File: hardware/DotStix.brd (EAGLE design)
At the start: 20.3 x 50 mm, 27 parts, among them IC2 SI1145, U1 ATMEGA328P-MU-QFN32, U2 TMP102

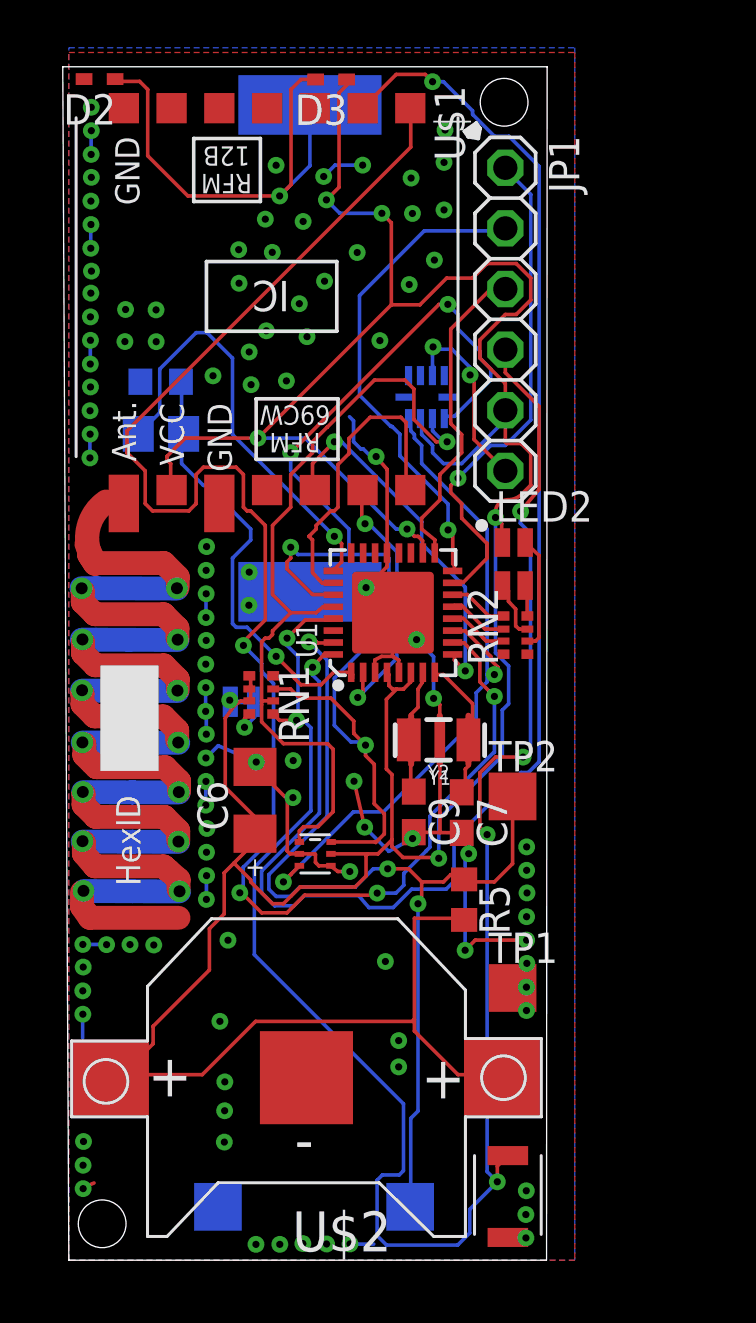
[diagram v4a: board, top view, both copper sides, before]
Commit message: Draft: add 9DoF motion sensor
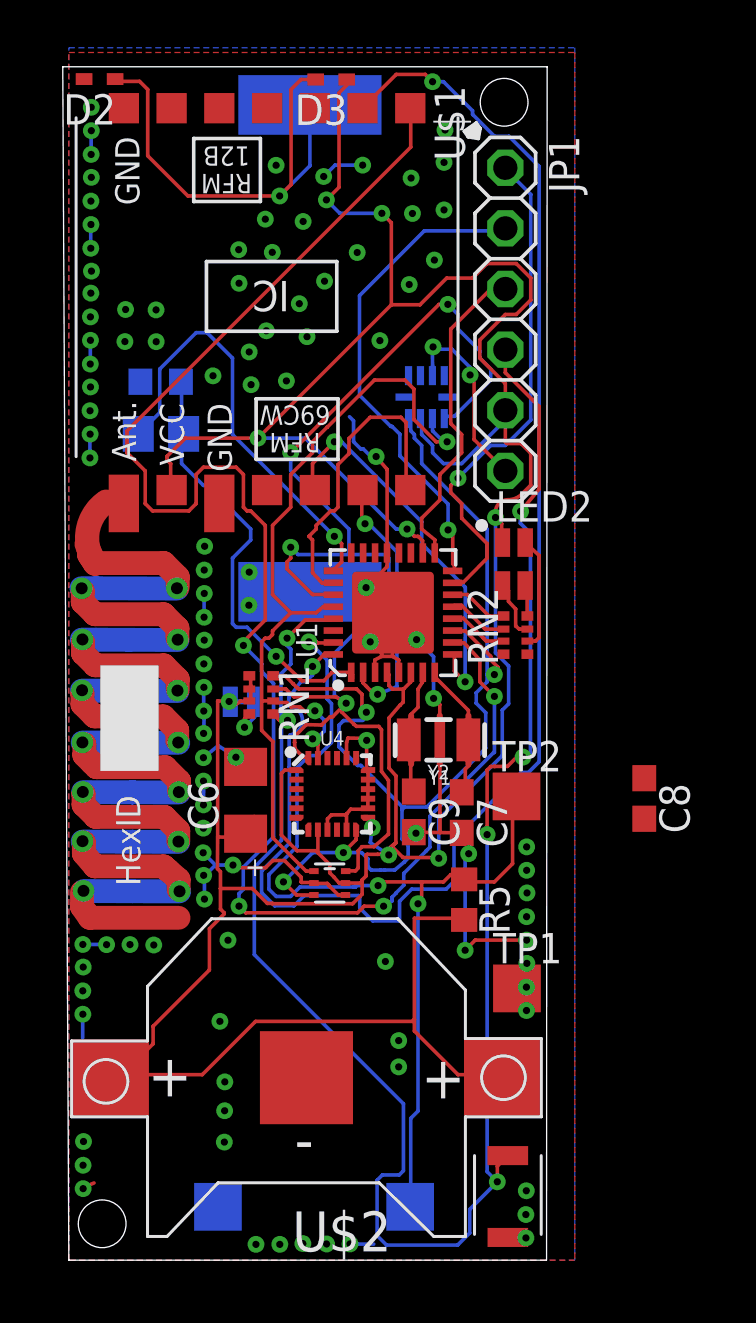
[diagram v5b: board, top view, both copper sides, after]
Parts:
- added C8: 0.1uF, resistor:C0603
- added U4: 9DoF IMU, SparkFun-Sensors:QFN24-3X3
- moved U2 1.37 mm to (10.9, 15.8)
- moved C6 0.39 mm to (7.41, 19.3)
- moved TP1 0.18 mm to (18.8, 11.4)
- moved TP2 0.17 mm to (18.8, 19.4)
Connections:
- new net N$11: C8.1, U4.10
- net +3V3: now also U4.1, U4.13, U4.8
- net GND: now also C8.2, U4.11, U4.18, U4.20, U4.9
- net INT_MULTIPLE: now also RN1.4, U4.12
- net SCL: now also U4.23
- net SDA: now also U4.24
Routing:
- net INT_MULTIPLE: track 29.3 -> 45.6 mm, vias 2 -> 4
- net +3V3: track 144.9 -> 158.2 mm, vias 7 -> 9
- net GND: track 71.9 -> 76.5 mm, vias 112 -> 110
- net SDA: track 49.8 -> 53.4 mm
- net SCL: track 33.8 -> 37.4 mm, vias 1 -> 3
- net XTAL2: track 5.11 -> 3.80 mm
- net RIRQ: track 62.1 -> 63.2 mm
- net RSDI: track 15.4 -> 16.3 mm
- net RST: track 79.6 -> 78.7 mm

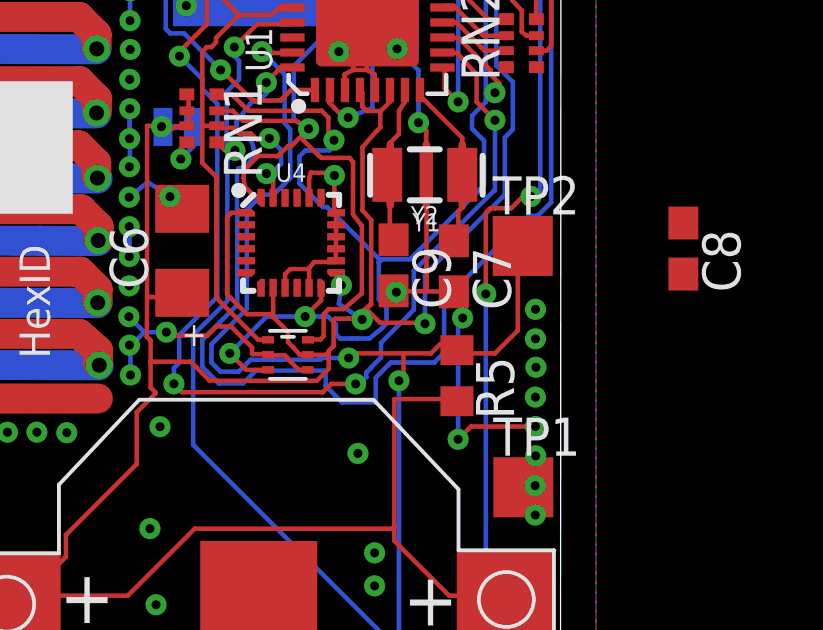
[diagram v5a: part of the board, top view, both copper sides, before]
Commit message: Draft:  9DoF pins connected, need to fix warnings
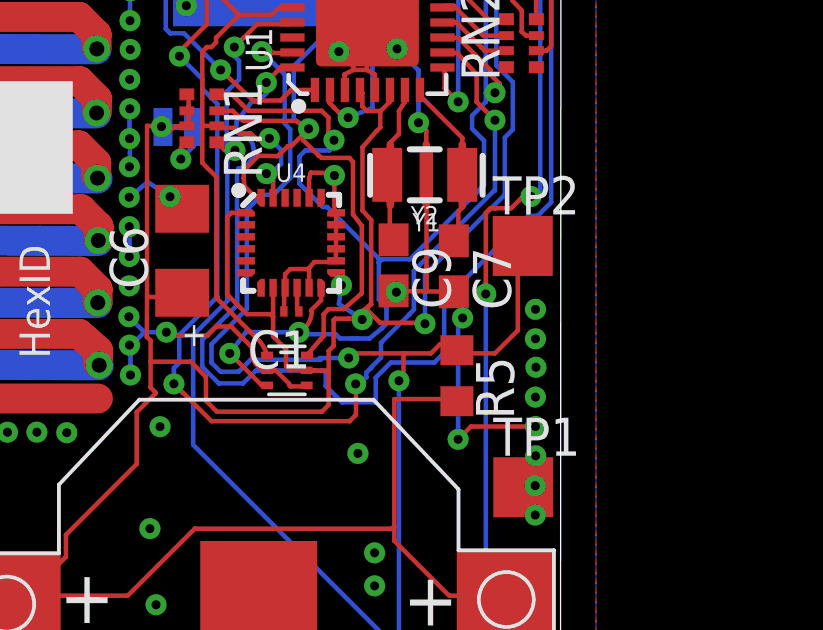
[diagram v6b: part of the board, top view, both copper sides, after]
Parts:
- removed C8: 0.1uF, resistor:C0603
- added C1: 0.1uF, rcl:C0201
- RN1: value (none) -> 4.7kΩ
- moved U2 0.52 mm to (10.9, 15.3)
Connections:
- net GND: now also C1.2; no longer C8.2
- net N$11: now also C1.1; no longer C8.1
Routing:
- net +3V3: track 158.2 -> 160.9 mm
- net RSDO: track 68.0 -> 69.4 mm
- net GND: track 76.5 -> 77.5 mm
- net N$11: track 0.00 -> 0.81 mm

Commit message: Add 9Dof: removed warnings
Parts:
- moved TP2 0.20 mm to (18.6, 19.4)
- moved TP1 0.20 mm to (18.6, 11.4)
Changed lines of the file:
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@@
 <element name="U$2" library="adafruit" package="CR1220-SMD" value="" x="9.9568" y="7.6454" rot="R180"/>
 <element name="JP1" library="adafruit" package="1X06" value="" x="18.288" y="39.4208" rot="R270"/>
-<element name="TP1" library="testpad" package="TP20SQ" value="TPTP20SQ" x="18.77568125" y="11.38681875">
-<attribute name="TP_SIGNAL_NAME" value="" x="18.77568125" y="11.38681875" size="1.778" layer="27" display="off"/>
+<element name="TP1" library="testpad" package="TP20SQ" value="TPTP20SQ" x="18.580103125" y="11.389359375">
+<attribute name="TP_SIGNAL_NAME" value="" x="18.580103125" y="11.389359375" size="1.778" layer="27" display="off"/>
 </element>
-<element name="TP2" library="testpad" package="TP20SQ" value="TPTP20SQ" x="18.7579" y="19.431">
-<attribute name="TP_SIGNAL_NAME" value="" x="18.7579" y="19.431" size="1.778" layer="27" display="off"/>
+<element name="TP2" library="testpad" package="TP20SQ" value="TPTP20SQ" x="18.56231875" y="19.433540625">
+<attribute name="TP_SIGNAL_NAME" value="" x="18.56231875" y="19.433540625" size="1.778" layer="27" display="off"/>
 </element>
 <element name="D1" library="SparkFun" package="SOLARBIT-12X1" value="SOLAR-IXYS-" x="10.101578125" y="38.204140625" rot="MR270"/>
@@
 <wire x1="8.5471" y1="16.74621875" x2="8.244840625" y2="16.443959375" width="0.1524" layer="1"/>
 <wire x1="8.244840625" y1="16.443959375" x2="6.990078125" y2="16.443959375" width="0.1524" layer="1"/>
-<wire x1="6.990078125" y1="16.443959375" x2="6.87831875" y2="16.55571875" width="0.1524" layer="1"/>
-<via x="6.87831875" y="16.55571875" extent="1-16" drill="0.3"/>
-<wire x1="6.87831875" y1="16.55571875" x2="6.1442625" y2="16.55571875" width="0.1524" layer="16"/>
+<wire x1="6.990078125" y1="16.443959375" x2="6.830059375" y2="16.197578125" width="0.1524" layer="1"/>
+<via x="6.830059375" y="16.197578125" extent="1-16" drill="0.3"/>
+<wire x1="6.830059375" y1="16.197578125" x2="6.1442625" y2="16.55571875" width="0.1524" layer="16"/>
 <wire x1="6.1442625" y1="16.55571875" x2="5.628640625" y2="17.071340625" width="0.1524" layer="16"/>
 <wire x1="5.68198125" y1="16.12391875" x2="5.7124625" y2="16.12391875" width="0.1524" layer="16"/>
@@
 <wire x1="18.288" y1="37.1856" x2="18.288" y2="38.1508" width="0.1524" layer="1"/>
 <wire x1="19.6977" y1="35.7759" x2="18.288" y2="37.1856" width="0.1524" layer="1"/>
-<wire x1="17.526" y1="17.8308" x2="17.490440625" y2="18.150840625" width="0.1524" layer="1"/>
+<wire x1="17.526" y1="17.8308" x2="17.490440625" y2="18.150840625" width="0" layer="19" extent="1-16"/>
 <wire x1="17.526" y1="3.7109375" x2="17.526" y2="17.8308" width="0.1524" layer="16"/>
 <via x="9.144" y="26.0604" extent="1-16" drill="0.3"/>
@@
 <wire x1="18.3769" y1="20.6883" x2="17.846040625" y2="20.6883" width="0.1524" layer="1"/>
 <wire x1="17.846040625" y1="20.6883" x2="17.8435" y2="20.685759375" width="0.1524" layer="1"/>
-<wire x1="17.8435" y1="20.685759375" x2="17.6784" y2="20.685759375" width="0.1524" layer="1"/>
-<wire x1="17.6784" y1="20.685759375" x2="17.526" y2="20.533359375" width="0.1524" layer="1"/>
-<wire x1="17.526" y1="20.533359375" x2="17.526" y2="17.8308" width="0.1524" layer="1"/>
 <wire x1="7.7724" y1="16.4592" x2="8.91031875" y2="17.59711875" width="0.1524" layer="16"/>
 <wire x1="8.91031875" y1="17.59711875" x2="8.91031875" y2="22.34691875" width="0.1524" layer="16"/>
@@
 <wire x1="8.887459375" y1="24.56688125" x2="8.887459375" y2="22.616159375" width="0.1524" layer="16"/>
 <wire x1="8.887459375" y1="22.616159375" x2="9.16431875" y2="22.616159375" width="0.1524" layer="16"/>
+<wire x1="17.8435" y1="20.685759375" x2="17.447259375" y2="20.685759375" width="0.1524" layer="1"/>
+<wire x1="17.447259375" y1="20.685759375" x2="17.2974" y2="20.5359" width="0.1524" layer="1"/>
+<wire x1="17.2974" y1="20.5359" x2="17.2974" y2="18.0594" width="0.1524" layer="1"/>
+<wire x1="17.2974" y1="18.0594" x2="17.526" y2="17.8308" width="0.1524" layer="1"/>
 </signal>
 <signal name="RSEL">
@@
 <via x="17.8308" y="23.622" extent="1-16" drill="0.3"/>
 <via x="7.3152" y="25.7556" extent="1-16" drill="0.3"/>
-<wire x1="7.30758125" y1="16.46428125" x2="7.30758125" y2="15.53718125" width="0.1524" layer="16"/>
 <wire x1="17.8308" y1="21.2725" x2="17.8308" y2="23.622" width="0.1524" layer="16"/>
 <wire x1="17.8308" y1="21.2725" x2="17.800321875" y2="21.2725" width="0.1524" layer="16"/>
@@
 <wire x1="8.0772" y1="24.665940625" x2="8.57758125" y2="24.165559375" width="0.1524" layer="16"/>
 <wire x1="8.57758125" y1="24.165559375" x2="8.57758125" y2="17.73428125" width="0.1524" layer="16"/>
-<wire x1="8.57758125" y1="17.73428125" x2="7.30758125" y2="16.46428125" width="0.1524" layer="16"/>
 <wire x1="13.7033" y1="15.3797" x2="13.7033" y2="15.367" width="0.1524" layer="16"/>
 <wire x1="13.7033" y1="15.367" x2="13.54328125" y2="15.20698125" width="0.1524" layer="16"/>
@@
 <wire x1="13.197840625" y1="13.79981875" x2="13.197840625" y2="14.8209" width="0.1524" layer="1"/>
 <wire x1="13.197840625" y1="14.8209" x2="13.18768125" y2="14.831059375" width="0.1524" layer="1"/>
+<wire x1="7.30758125" y1="15.53718125" x2="7.30758125" y2="15.547340625" width="0.1524" layer="16"/>
+<wire x1="7.30758125" y1="15.547340625" x2="7.4422" y2="15.681959375" width="0.1524" layer="16"/>
+<wire x1="7.4422" y1="15.681959375" x2="7.4422" y2="16.5989" width="0.1524" layer="16"/>
+<wire x1="7.4422" y1="16.5989" x2="8.57758125" y2="17.73428125" width="0.1524" layer="16"/>
 </signal>
 <signal name="RIRQ">
@@
 <contactref element="U4" pad="8"/>
 <wire x1="12.28851875" y1="15.930878125" x2="12.45361875" y2="16.095978125" width="0.1524" layer="1"/>
-<wire x1="6.2255375" y1="16.40331875" x2="6.2357" y2="17.731740625" width="0.1524" layer="1"/>
-<wire x1="6.2357" y1="17.731740625" x2="6.2357" y2="23.434040625" width="0.1524" layer="1"/>
+<wire x1="6.240778125" y1="16.40331875" x2="6.238240625" y2="17.731740625" width="0.1524" layer="1"/>
+<wire x1="6.238240625" y1="17.731740625" x2="6.2357" y2="23.434040625" width="0.1524" layer="1"/>
 <wire x1="6.2357" y1="23.434040625" x2="6.715759375" y2="23.408640625" width="0.1524" layer="1"/>
 <via x="6.715759375" y="23.408640625" extent="1-16" drill="0.3"/>
@@
 <wire x1="6.581140625" y1="23.41118125" x2="6.76401875" y2="23.395940625" width="0.1524" layer="16"/>
 <wire x1="7.62" y1="17.34058125" x2="7.25678125" y2="17.7038" width="0.1524" layer="1"/>
-<wire x1="7.25678125" y1="17.7038" x2="6.2357" y2="17.731740625" width="0.1524" layer="1"/>
+<wire x1="7.25678125" y1="17.7038" x2="6.238240625" y2="17.731740625" width="0.1524" layer="1"/>
 <wire x1="10.43630625" y1="18.035140625" x2="10.43630625" y2="17.069353125" width="0.1524" layer="1"/>
 <wire x1="12.58880625" y1="18.535140625" x2="12.70761875" y2="18.535140625" width="0.1524" layer="1"/>
-<wire x1="12.70761875" y1="18.535140625" x2="12.715240625" y2="18.1229" width="0.1524" layer="1"/>
-<via x="12.715240625" y="18.1229" extent="1-16" drill="0.3"/>
-<wire x1="12.715240625" y1="18.1229" x2="12.62888125" y2="17.498059375" width="0.1524" layer="16"/>
+<wire x1="12.70761875" y1="18.535140625" x2="12.7736625" y2="18.176240625" width="0.1524" layer="1"/>
+<via x="12.7736625" y="18.176240625" extent="1-16" drill="0.3"/>
+<wire x1="12.7736625" y1="18.176240625" x2="12.62888125" y2="17.498059375" width="0.1524" layer="16"/>
 <wire x1="12.62888125" y1="17.498059375" x2="13.40358125" y2="16.979896875" width="0.1524" layer="16"/>
 <via x="13.40358125" y="16.979896875" extent="1-16" drill="0.3"/>
@@
 <wire x1="6.51001875" y1="14.554203125" x2="6.352540625" y2="14.71168125" width="0.1524" layer="1"/>
 <wire x1="6.352540625" y1="14.71168125" x2="6.352540625" y2="15.572740625" width="0.1524" layer="1"/>
-<wire x1="6.352540625" y1="15.572740625" x2="6.352540625" y2="16.276315625" width="0.1524" layer="1"/>
-<wire x1="6.352540625" y1="16.276315625" x2="6.2255375" y2="16.40331875" width="0.1524" layer="1"/>
 <wire x1="7.69111875" y1="15.572740625" x2="6.352540625" y2="15.572740625" width="0.1524" layer="1"/>
 <wire x1="9.48380625" y1="20.535140625" x2="9.046721875" y2="20.535140625" width="0.1524" layer="1"/>
@@
 <wire x1="10.99311875" y1="15.288259375" x2="11.55151875" y2="15.288259375" width="0.1524" layer="1"/>
 <wire x1="11.55151875" y1="15.288259375" x2="11.5566" y2="15.283178125" width="0.1524" layer="1"/>
+<wire x1="6.240778125" y1="16.40331875" x2="6.23315625" y2="15.69974375" width="0.1524" layer="1"/>
+<wire x1="6.23315625" y1="15.69974375" x2="6.352540625" y2="15.572740625" width="0.1524" layer="1"/>
 <wire x1="6.76401875" y1="23.395940625" x2="6.939278125" y2="23.238459375" width="0" layer="19" extent="1-16"/>
 </signal>
@@
 <wire x1="18.5928" y1="16.6116" x2="18.590259375" y2="18.823940625" width="0.1524" layer="1"/>
 <wire x1="18.590259375" y1="18.823940625" x2="18.590259375" y2="19.431" width="0.1524" layer="1"/>
-<wire x1="18.590259375" y1="19.431" x2="18.7579" y2="19.431" width="0.1524" layer="1"/>
+<wire x1="18.590259375" y1="19.431" x2="18.56231875" y2="19.433540625" width="0.1524" layer="1"/>
 <wire x1="17.8308" y1="15.8496" x2="18.5928" y2="16.6116" width="0.1524" layer="1"/>
 <wire x1="16.6116" y1="15.8496" x2="17.8308" y2="15.8496" width="0.1524" layer="1"/>
